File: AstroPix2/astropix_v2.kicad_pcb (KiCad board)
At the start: 4 copper layers, 51.3 x 34.2 mm, 41 parts, among them J1 pcie_con, J10 SPI_right, J2 VDD_JP, J3 Vtemp1, J4 SFOut, J5 sample_clock_out, J6 HV_in_external, J7 Conn_01x03, J8 Conn_01x03, J9 SPI_left, U1 OPA320, U2 SN65LVDS4, U3 OPA320, U4 AstroPix2_split

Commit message: PCB: Updated AstroPix2 Schematic
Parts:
- removed H3, H4: MountingHole, MountingHole:MountingHole_3.2mm_M3
- removed J2: VDD_JP, Connector_PinHeader_2.54mm:PinHeader_1x03_P2.54mm_Vertical
- removed J7: Conn_01x03, Connector_PinHeader_2.54mm:PinHeader_1x03_P2.54mm_Vertical
- removed R10: 1k, Resistor_SMD:R_0603_1608Metric
- added FID1: Fiducial, Fiducial:Fiducial_1mm_Mask2mm, F.Cu at (108.0, 54.6)
- added FID2: Fiducial, Fiducial:Fiducial_1mm_Mask2mm, F.Cu at (154.3, 100.3)
- added JP1: VDD_JP, Connector_PinHeader_2.54mm:PinHeader_1x03_P2.54mm_Vertical, F.Cu at (114.3, 92.1)
- added Logo1: KIT_logo, astropix:logo, F.Cu at (114.6, 54.7)
- added R11: 1k, Resistor_SMD:R_0603_1608Metric, F.Cu at (110.6, 99.7)
- added R12: 1k, Resistor_SMD:R_0603_1608Metric, F.Cu at (108.0, 87.6)
- added R13: NC, Resistor_SMD:R_0603_1608Metric, F.Cu at (124.7, 82.5)
- added R14: NC, Resistor_SMD:R_0603_1608Metric, F.Cu at (128.0, 82.5)
- added R15: 1k, Resistor_SMD:R_0603_1608Metric, F.Cu at (176.6, 75.9)
- added R16: 2k, Resistor_SMD:R_0603_1608Metric, F.Cu at (180.6, 73.4)
- C3, C4: value .1uF -> 1nF; footprint Capacitor_SMD:C_0603_1608Metric -> Capacitor_SMD:C_1210_3225Metric
- C5, C6: footprint Capacitor_SMD:C_0603_1608Metric -> Capacitor_SMD:C_1210_3225Metric
- J1: value pcie_con -> pcie_GECCO
- J8: value Conn_01x03 -> VBias
- R1: value 1k -> 0; footprint Resistor_SMD:R_0603_1608Metric -> Resistor_SMD:R_1206_3216Metric
- R2: value 22 -> 47
- R9: value 10k -> 680
- U1: value OPA320 -> TLV333; footprint Package_TO_SOT_SMD:SOT-23-5 -> Package_TO_SOT_SMD:SOT-23-6
- U3: value OPA320 -> OPA320S; footprint Package_TO_SOT_SMD:SOT-23-5 -> Package_TO_SOT_SMD:SOT-23-6
- moved C4 121.9 mm to (111.8, 86.4), turned to 270 degrees
- moved C5 118.6 mm to (109.9, 92.1), turned to 180 degrees
- moved Cvdd2 116.7 mm to (118.5, 90.7)
- moved Cvdd3 116.6 mm to (118.5, 92.6)
- moved R8 114.0 mm to (119.0, 83.2), turned to 270 degrees
- moved Cvdd1 109.9 mm to (118.5, 88.8)
- moved R1 108.9 mm to (107.0, 100.2), turned to 270 degrees
- moved R5 105.5 mm to (131.3, 93.7), turned to 180 degrees
- moved J10 99.0 mm to (130.2, 54.6), turned to 90 degrees
- moved C3 98.2 mm to (109.9, 95.9), turned to 180 degrees
- moved R3 93.9 mm to (121.5, 85.5)
- moved J9 91.5 mm to (108.0, 59.7)
- moved Cvdda3 90.4 mm to (120.8, 96.1), turned to 90 degrees
- moved C2 88.4 mm to (144.9, 83.8)
- moved Cvdda1 87.1 mm to (116.9, 96.1), turned to 90 degrees
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- renumbered C7 to Cvdd1, C8 to Cvdd2, C13 to Cvdd3, C9 to Cvdda1, C10 to Cvdda2, C11 to Cvdda3
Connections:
- C3 pad 2: suba -> subd
- C5 pad 2: suba -> subd
- J1 pad A1: (no net) -> -HV
- J1 pad A11: (no net) -> GND
- J1 pad A16: (no net) -> /spi_left_clk
- J1 pad A17: (no net) -> /spi_left_csn
- J1 pad A18: (no net) -> /spi_left_miso1
- J1 pad A19: (no net) -> /spi_left_miso0
- J1 pad A20: (no net) -> /spi_left_mosi
- J1 pad A24: (no net) -> /sr_ck1
- J1 pad A25: (no net) -> /sr_ck2
- J1 pad A28: (no net) -> /Inj
- J1 pad B1: (no net) -> -HV
- J1 pad B11: (no net) -> GND
- J1 pad B16: (no net) -> /sample_clock_se_P
- J1 pad B17: (no net) -> /sample_clock_se_N
- J1 pad B18: (no net) -> /sample_clock_P
- J1 pad B19: (no net) -> /sample_clock_N
- J1 pad B20: (no net) -> /timestamp_clk
- J1 pad B21: (no net) -> /interrupt
- J1 pad B22: (no net) -> /res_n
- J1 pad B23: (no net) -> /hold
- J1 pad B24: (no net) -> /sr_ld
- J1 pad B25: (no net) -> /sr_sin
- J1 pad B3: (no net) -> /VDD18_in
- J1 pad B32: (no net) -> /DAC_blpix
- J1 pad B33: (no net) -> /DAC_VCasc2!
- J1 pad B34: (no net) -> /DAC_ThPix
- J1 pad B35: (no net) -> /DAC_vminuspix
- J1 pad B4: (no net) -> /VDD18_in
- J1 pad B5: (no net) -> /POW4_in
- J1 pad B6: (no net) -> /POW4_in
- J1 pad B7: (no net) -> VDDA
- J1 pad B8: (no net) -> VDDA
- J10 pad 1: (no net) -> /spi_right_clk
- J10 pad 2: (no net) -> /spi_right_miso1
- J10 pad 3: (no net) -> /spi_right_miso0
- J10 pad 4: (no net) -> /spi_right_csn
- J10 pad 5: (no net) -> /spi_right_mosi
- J5 pad 1: /sr_sout -> /sc_out
- J8 pad 1: Net-(J8-Pad1) -> /pamp
- J8 pad 2: Net-(J8-Pad2) -> /VPBias
- J9 pad 1: (no net) -> /spi_left_mosi
- J9 pad 2: (no net) -> /spi_left_miso0
- J9 pad 3: (no net) -> /spi_left_miso1
- J9 pad 4: (no net) -> /spi_left_clk
- J9 pad 5: (no net) -> /spi_left_csn
- R1 pad 1: suba -> Net-(J6-Pad1)
- R1 pad 2: (no net) -> -HV
- R2 pad 2: Net-(R2-Pad2) -> Net-(R16-Pad2)
- R8 pad 1: Net-(R8-Pad1) -> /sample_clock_se_in
- R8 pad 2: VDDA -> /sample_clock_se_P
- R9 pad 1: /sr_rb -> Net-(R9-Pad1)
- R9 pad 2: GND -> /Vtemp1
- U1 pad 1: Net-(R2-Pad2) -> Net-(R16-Pad2)
- U1 pad 3: /Vtemp1 -> Net-(R9-Pad1)
- U1 pad 4: Net-(R2-Pad2) -> Net-(R15-Pad1)
- U2 pad 8: (no net) -> /sample_clock_se_in
- U4 pad B1: suba -> subd
- U4 pad B17: /sr_rb -> GND
- U4 pad B18: /sr_sout -> (no net)
- U4 pad B2: suba -> subd
- U4 pad B23: Net-(J8-Pad2) -> GND
- U4 pad B24: Net-(J8-Pad1) -> /VPBias
- U4 pad B25: /DAC_blpix -> /pamp
- U4 pad B26: Net-(U4-PadB26) -> /DAC_blpix
- U4 pad B27: GND -> (no net)
- U4 pad B28: VDDA -> GND
- U4 pad B29: /Inj -> VDDA
- U4 pad B30: /DAC_VCasc2! -> /Inj
- U4 pad B31: /DAC_ThPix -> /DAC_VCasc2!
- U4 pad B32: /DAC_vminuspix -> /DAC_ThPix
- U4 pad B33: GND -> /DAC_vminuspix
- U4 pad B34: VDDA -> GND
- U4 pad B35: /SFOut -> VDDA
- U4 pad B36: Net-(R8-Pad1) -> /SFOut
- U4 pad B37: GND -> VDDA
- U4 pad B38: /Vtemp1 -> GND
- U4 pad B39: suba -> /Vtemp1
- U4 pad B45: (no net) -> suba
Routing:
- net /spi_left_mosi: track 0.00 -> 57.0 mm, vias 0 -> 1
- net /spi_left_miso0: track 0.00 -> 53.0 mm, vias 0 -> 1
- net /spi_left_miso1: track 0.00 -> 49.5 mm, vias 0 -> 1
- net /spi_left_csn: track 0.00 -> 47.6 mm, vias 0 -> 1
- net /spi_left_clk: track 0.00 -> 47.5 mm, vias 0 -> 1
- net /DAC_vminuspix: track 0.00 -> 33.6 mm
- net /Inj: track 0.00 -> 31.4 mm, vias 0 -> 1
- net /sr_sin: track 0.00 -> 31.3 mm
- net /hold: track 0.00 -> 31.1 mm
- net /DAC_ThPix: track 0.00 -> 31.1 mm
- net /DAC_blpix: track 0.00 -> 31.0 mm
- net /sr_ld: track 0.00 -> 30.5 mm
- net /sr_ck1: track 0.00 -> 29.6 mm, vias 0 -> 1
- net /DAC_VCasc2!: track 0.00 -> 29.1 mm
- net /sample_clock_N: track 0.00 -> 27.8 mm
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- added copper zone on In1.Cu, net GND
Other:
- board size 51.3 x 34.2 mm -> 51.3 x 48.8 mm
- net class Default: via_dia 0.6 -> 0.45; via_drill 0.3 -> 0.15
- net class sampleclock_diff added: clearance 0.125, trace_width 0.125, via_dia 0.45, via_drill 0.15
- rule via_min_drill: 0.3 -> 0.15
- rule via_min_size: 0.4 -> 0.45
- board text added: "ADL"
- board text added: "Nicolas Striebig Juni 2021"

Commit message: PCB: First astropix2 layout
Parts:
- removed Cvdda1: 1nF, Capacitor_SMD:C_0603_1608Metric
- removed Cvdda2: .1uF, Capacitor_SMD:C_0603_1608Metric
- removed Cvdda3: 10uF, Capacitor_SMD:C_0603_1608Metric
- removed R13, R14: NC, Resistor_SMD:R_0603_1608Metric
- removed R8: 0, Resistor_SMD:R_0603_1608Metric
- added C11: 1nF, Capacitor_SMD:C_0603_1608Metric, F.Cu at (117.6, 96.1)
- added C13: .1uF, Capacitor_SMD:C_0603_1608Metric, F.Cu at (119.2, 96.1)
- added C14: 10uF, Capacitor_SMD:C_0603_1608Metric, F.Cu at (120.8, 96.1)
- added C7: .1uF, Capacitor_SMD:C_0603_1608Metric, F.Cu at (118.8, 83.6)
- added G***: LOGO, astropix:hv, F.Cu at (114.3, 83.4)
- R15: value 1k -> 2.2k
- R16: value 2k -> 2.2k
- R3, R4: footprint Resistor_SMD:R_0603_1608Metric -> Resistor_SMD:R_0402_1005Metric
- R9: value 680 -> 1k
- moved R16 39.5 mm to (144.5, 89.4), turned to 180 degrees
- moved R9 38.9 mm to (140.5, 87.8), turned to 180 degrees
- moved R15 31.2 mm to (147.3, 86.7), turned to 90 degrees
- moved C12 13.0 mm to (123.6, 83.7), turned to 270 degrees
- moved R11 8.27 mm to (107.3, 92.1), turned to 270 degrees
- moved C1 5.18 mm to (144.4, 75.6), turned to 180 degrees
- moved C6 5.01 mm to (110.7, 87.5), turned to 90 degrees
- moved U3 4.96 mm to (144.3, 78.5)
- moved R7 4.32 mm to (128.5, 92.3), turned to 90 degrees
- moved C8 3.95 mm to (120.8, 92.0), turned to 270 degrees
- moved C4 2.51 mm to (114.0, 87.5), turned to 90 degrees
- moved R1 2.22 mm to (107.2, 97.9)
- moved R2 2.10 mm to (144.5, 91.0)
- moved R5 1.89 mm to (130.0, 92.3), turned to 90 degrees
- moved J4 1.78 mm to (152.4, 74.4)
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- renumbered Cvdd3 to C10, Cvdd1 to C8, Cvdd2 to C9
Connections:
- net Net-(J6-Pad1) renamed /HV_in_ext
- C1 pad 1: VDD -> VDDA
- C2 pad 1: VDD -> VDDA
- J1 pad A40: (no net) -> /spi_right_miso1
- J1 pad A41: (no net) -> /spi_right_miso0
- J1 pad A42: (no net) -> /spi_right_csn
- J1 pad A43: (no net) -> /spi_right_mosi
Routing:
- net /spi_right_miso1: track 0.63 -> 64.2 mm, vias 0 -> 1
- net /spi_right_miso0: track 0.31 -> 61.8 mm, vias 0 -> 1
- net /spi_right_csn: track 1.51 -> 61.5 mm, vias 0 -> 1
- net /spi_right_mosi: track 1.39 -> 59.8 mm, vias 0 -> 1
- net GND: track 0.00 -> 30.2 mm, vias 0 -> 30
- net /spi_right_clk: track 1.93 -> 31.2 mm
- net VDDA: track 3.64 -> 31.5 mm, vias 2 -> 7
- net (no net): track 26.9 -> 0.00 mm
- net /HV_in_ext: track 0.00 -> 20.5 mm
- net /res_n: track 13.2 -> 32.0 mm, vias 0 -> 2
- net /interrupt: track 11.1 -> 27.9 mm
- net VDD: track 1.64 -> 18.3 mm, vias 1 -> 7
- net /VDD18_in: track 0.00 -> 16.4 mm
- net subd: track 0.00 -> 14.4 mm, vias 0 -> 2
- net -HV: track 0.00 -> 12.7 mm, vias 0 -> 1
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- added copper zone on B.Cu, net GND
- added copper zone on F.Cu, net GND
- added copper zone on In2.Cu, net VDD
- added copper zone on In2.Cu, net VDDA
- added copper zone on In2.Cu, net suba
- added copper zone on In2.Cu, net subd
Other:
- net class pow added: clearance 0.125, trace_width 0.4, via_dia 0.45, via_drill 0.15
- net class sub added: clearance 0.5, trace_width 0.15, via_dia 0.45, via_drill 0.15
- net class vdd added: clearance 0.125, trace_width 0.25, via_dia 0.45, via_drill 0.15
- net class vdda added: clearance 0.125, trace_width 0.25, via_dia 0.45, via_drill 0.15
- board text added: "AstroPix2"
- board text added: "N. Striebig Juli 2021"
- board text removed: "Nicolas Striebig Juni 2021"

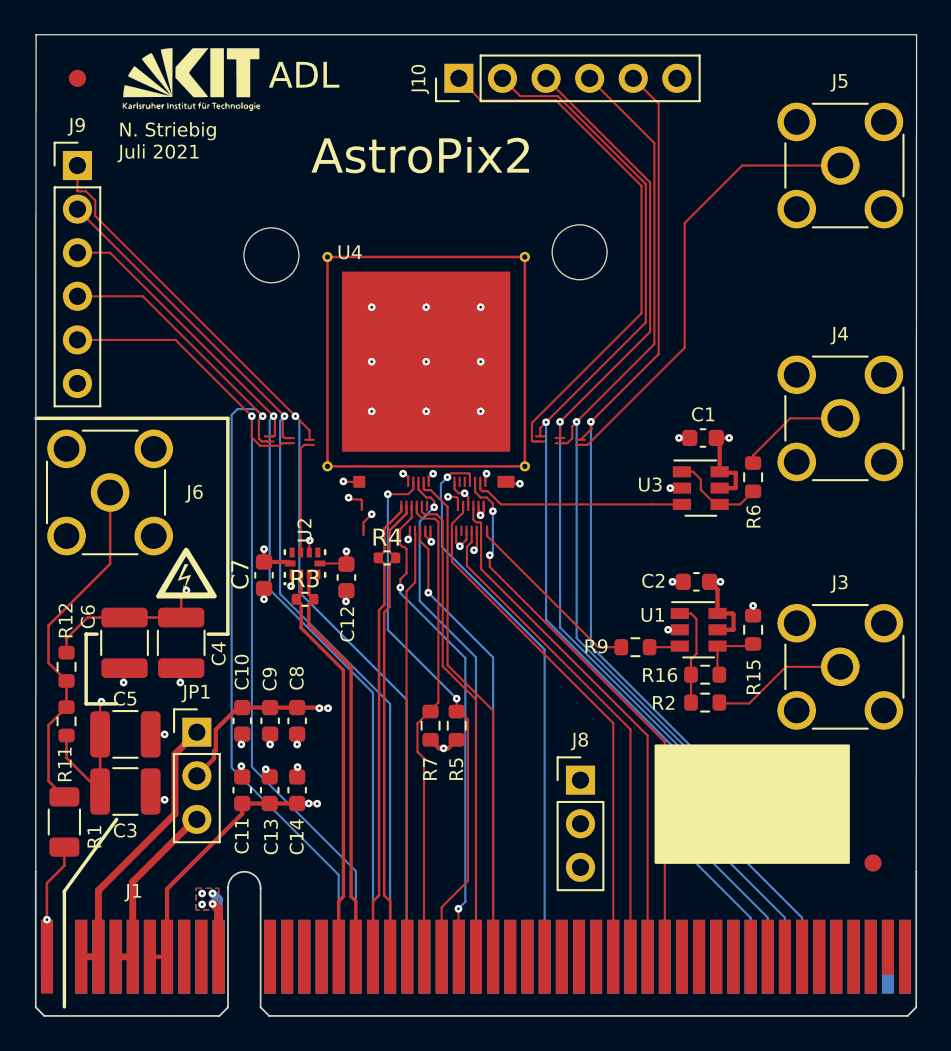
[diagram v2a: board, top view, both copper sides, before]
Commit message: PCB: Updated astropix2 pcb
-diff pair impedance
-added teardropds
-small fixes
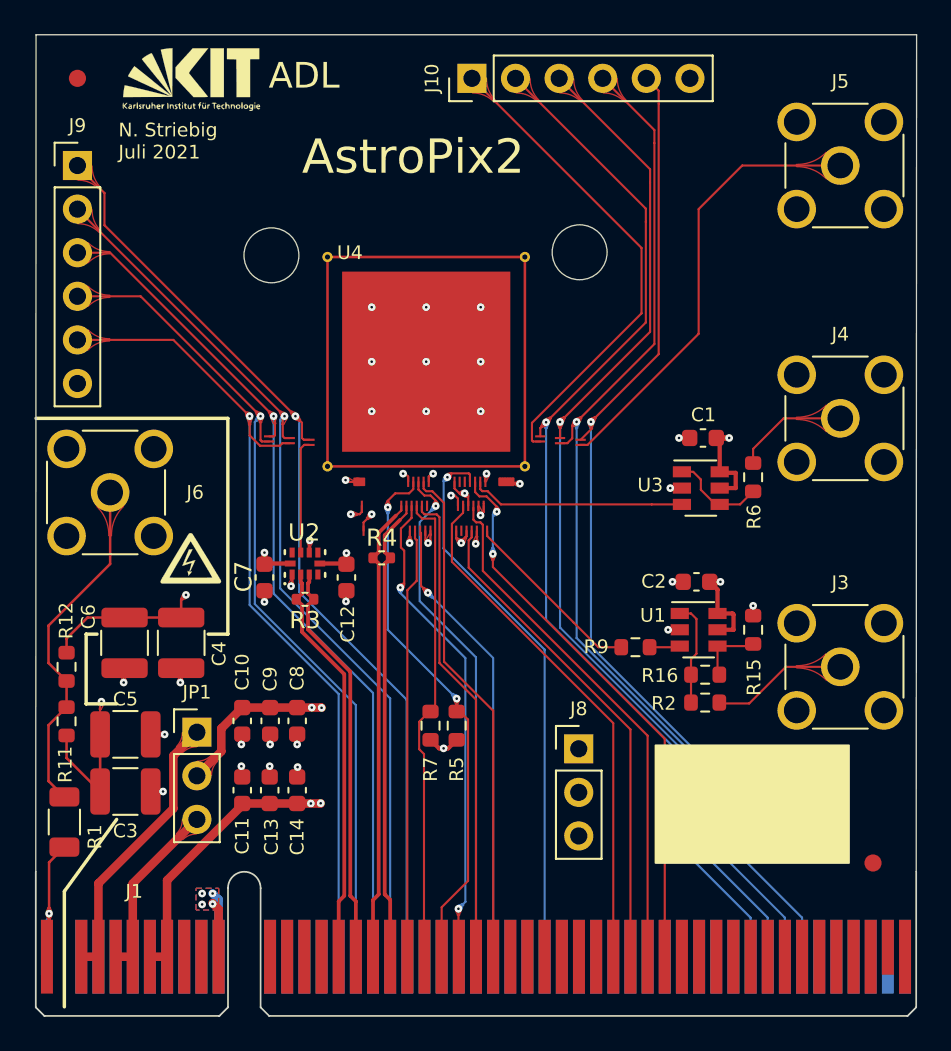
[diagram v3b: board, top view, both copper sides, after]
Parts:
- removed G***: LOGO, astropix:hv
- added Logo2: HV_logo, astropix:hv, F.Cu at (114.6, 82.6)
- C8: value 1n -> 1nF
- moved J8 1.83 mm to (137.2, 93.7)
- moved J10 0.76 mm to (130.9, 54.6)
- moved R4 0.30 mm to (125.7, 82.5)
- moved C7 0.13 mm to (118.8, 83.7)
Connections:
- J1 pad A16: /spi_left_clk -> /spi_left_csn
- J1 pad A17: /spi_left_csn -> /spi_left_clk
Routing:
- net VDD: track 18.3 -> 23.7 mm
- net -HV: track 12.7 -> 8.82 mm
- net /spi_right_clk: track 31.2 -> 28.3 mm
- net /spi_left_clk: track 52.0 -> 49.6 mm
- net /spi_right_miso1: track 64.2 -> 62.6 mm
- net VDDA: track 31.5 -> 33.0 mm
- net GND: track 30.2 -> 29.5 mm
- net /res_n: track 32.0 -> 31.4 mm
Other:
- net class clock_diff added: clearance 0.125, trace_width 0.125, via_dia 0.45, via_drill 0.15
- net class sampleclock_diff removed
